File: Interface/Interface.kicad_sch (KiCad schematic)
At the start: 0 parts

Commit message: Finished the Design of Peripheral Circuit
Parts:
- added C1, C15, C16, C17, C24: 1u, symbol Device:C
- added C10, C13, C18, C21, C25, C3, C31, C32, C33, C9: 4.7u, symbol Device:C
- added C11, C12, C14, C19, C2, C20, C22, C23, C26, C4, C5, C6, C7, C8: 0.22u, symbol Device:C
- added C27, C28, C29, C30: 100n, symbol Device:C
- added L1: 4.7u, symbol Device:L
- added R1: 30k, symbol Device:R
- added U1: MIMXRT1011DAE5A, Package_QFP:LQFP-80_12x12mm_P0.5mm, symbol utils:MIMXRT1011DAE5A
- added U2: LM809, Package_TO_SOT_SMD:SOT-23, symbol Power_Supervisor:LM809
- added Y1: 24M, symbol Device:Crystal_GND24
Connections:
- new net: U1.22 (POR_B), U2.2 (~{RESET})
- new net: C16.1, U1.37 (XTALI), Y1.1
- new net: C17.1, U1.38 (XTALO), Y1.3
- new net: C23.1, R1.1, U1.15 (DCDC_PSWITCH)
- new net: L1.1, U1.19 (DCDC_LP)
- new net: C10.1, C11.1, U1.35 (VDD_HIGH_CAP)
- new net: C25.1, C26.1, U1.31 (VDD_USB_CAP)
- new net: U1.16 (VSS_1), U1.30 (VSS_2), U1.34 (NGND_KEL0), U1.54 (VSS_3), U1.78 (VSS_4)
- new net: C14.1, U1.26 (VDD_SNVS_CAP)
- new net: C12.1, C13.1, U1.40 (NVCC_PLL)
- new net +3.3V: C1.1, C15.1, C18.1, C19.1, C2.1, C20.1, C27.1, C28.1, C29.1, C3.1, C30.1, C31.1, C32.1, C33.1, C4.1, C5.1, R1.2, U1.17 (DCDC_IN_Q), U1.18 (DCDC_IN), U1.25 (VDD_SNVS_IN), U1.39 (VDD_HIGH_IN), U1.42 (VDDA_ADC_3P3/ADC_VREFH), U1.50 (NVCC_GPIO_2), U1.63 (NVCC_GPIO_3), U1.7 (NVCC_GPIO_1), U1.71 (NVCC_GPIO_4), U2.3 (VCC)
- new net GND: C1.2, C10.2, C11.2, C12.2, C13.2, C14.2, C15.2, C16.2, C17.2, C18.2, C19.2, C2.2, C20.2, C21.2, C22.2, C23.2, C24.2, C25.2, C26.2, C27.2, C28.2, C29.2, C3.2, C30.2, C31.2, C32.2, C33.2, C4.2, C5.2, C6.2, C7.2, C8.2, C9.2, U1.20 (DCDC_GND), U1.23 (TEST_MODE), U1.27 (RTC_XTALI), U1.41 (VSSA_ADC_3P3/ADC_VREFL), U2.1 (GND), Y1.2, Y1.4
- new net VBUS: C24.1, U1.29 (USB_OTG1_VBUS)
- new net VDD: C21.1, C22.1, C6.1, C7.1, C8.1, C9.1, L1.2, U1.14 (VDD_SOC_IN_3/DCDC_SENSE), U1.53 (VDD_SOC_IN_1), U1.77 (VDD_SOC_IN_2)
- no-connect marks 0 -> 4

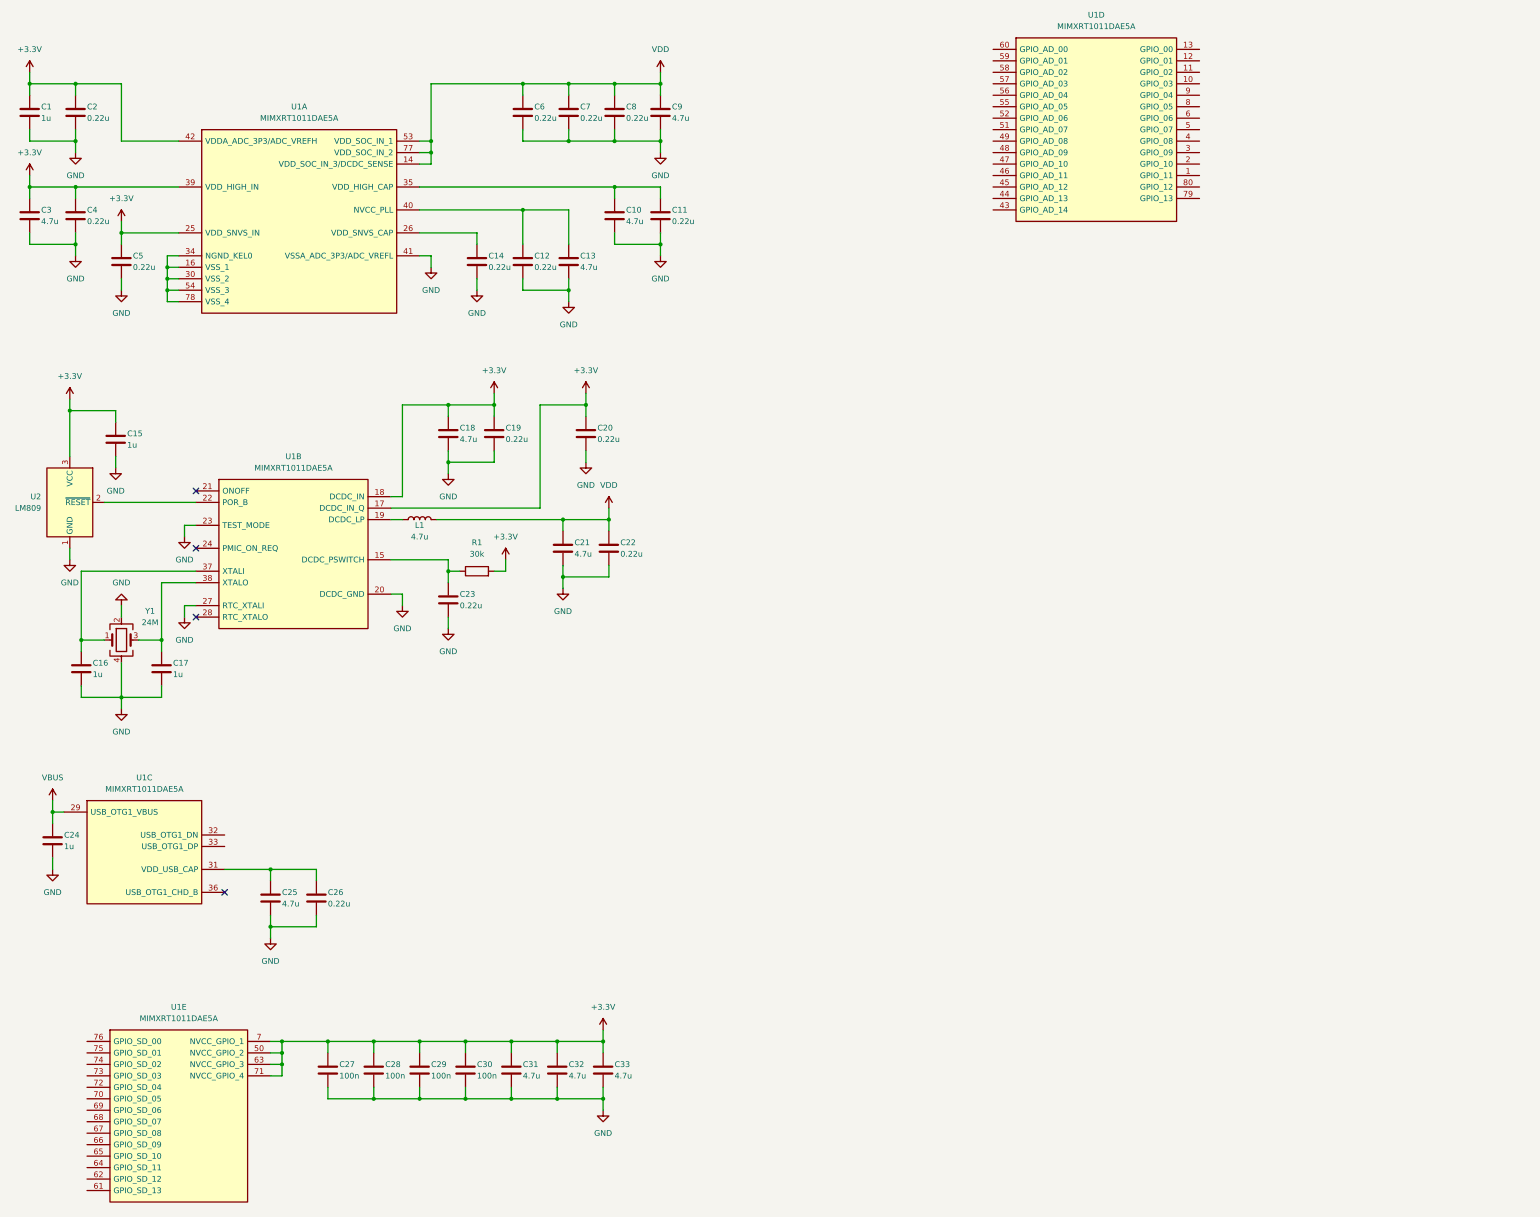
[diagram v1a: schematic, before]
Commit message: Finished Circuit Design of External Flash, Power Supply, etc.
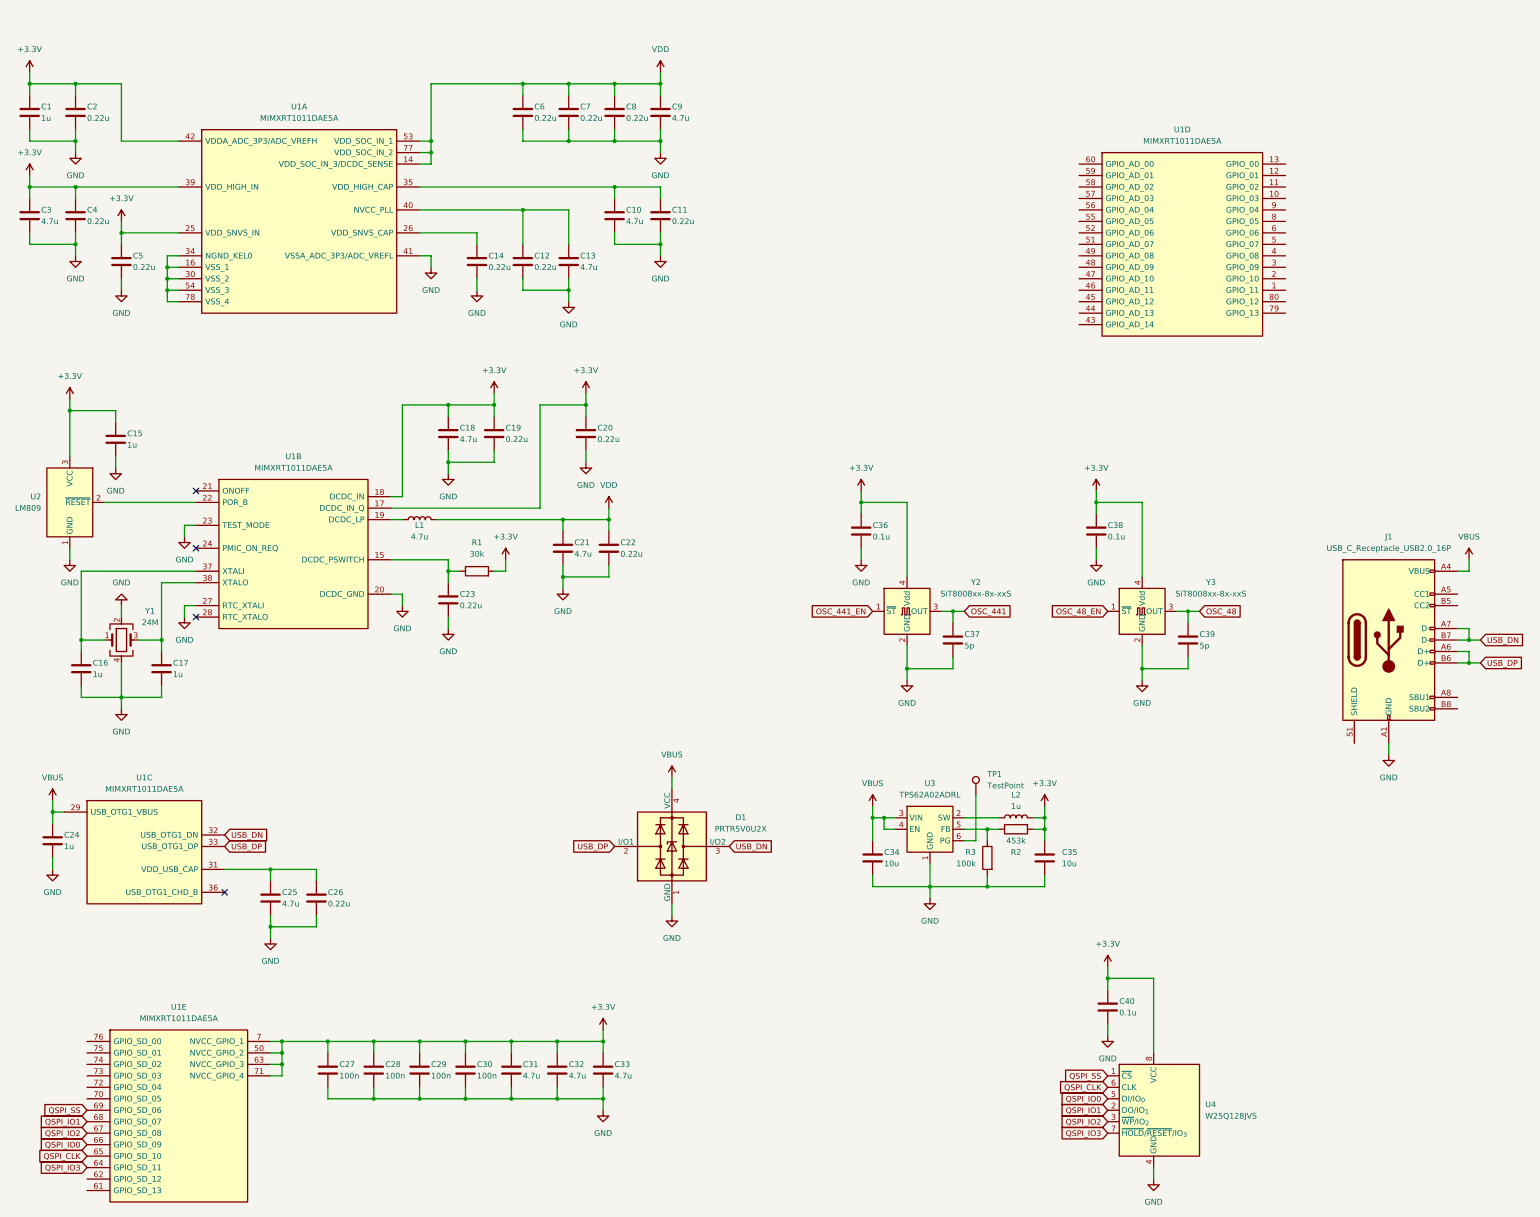
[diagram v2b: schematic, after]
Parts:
- added C34, C35: 10u, symbol Device:C
- added C36, C38, C40: 0.1u, symbol Device:C
- added C37, C39: 5p, symbol Device:C
- added D1: PRTR5V0U2X, Package_TO_SOT_SMD:SOT-143, symbol Power_Protection:PRTR5V0U2X
- added J1: USB_C_Receptacle_USB2.0_16P, symbol Connector:USB_C_Receptacle_USB2.0_16P
- added L2: 1u, symbol Device:L
- added R2: 453k, symbol Device:R
- added R3: 100k, symbol Device:R
- added TP1: TestPoint, TestPoint:TestPoint_Pad_D2.0mm, symbol Connector:TestPoint
- added U3: TPS62A02ADRL, Package_TO_SOT_SMD:SOT-563, symbol Regulator_Switching:TPS62A02ADRL
- added U4: W25Q128JVS, Package_SO:SOIC-8_5.3x5.3mm_P1.27mm, symbol Memory_Flash:W25Q128JVS
- added Y2, Y3: SiT8008xx-8x-xxS, Oscillator:Oscillator_SMD_SiT_PQFN-4Pin_7.0x5.0mm, symbol Oscillator:SiT8008xx-8x-xxS
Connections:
- net +3.3V: now also C35.1, C36.1, C38.1, C40.1, L2.2, R2.2, U4.8 (VCC), Y2.4 (Vdd), Y3.4 (Vdd)
- net GND: now also C34.2, C35.2, C36.2, C37.2, C38.2, C39.2, C40.2, D1.1 (GND), J1.A1 (GND), J1.A12 (GND), J1.B1 (GND), J1.B12 (GND), R3.2, U3.1 (GND), U4.4 (GND), Y2.2 (GND), Y3.2 (GND)
- net VBUS: now also C34.1, D1.4 (VCC), J1.A4 (VBUS), J1.A9 (VBUS), J1.B4 (VBUS), J1.B9 (VBUS), U3.3 (VIN), U3.4 (EN)
- net QSPI_IO3: now reaches U1.64 (GPIO_SD_11)
- net QSPI_IO3: now also U4.7 (~{HOLD}/~{RESET}/IO_{3})
- net QSPI_CLK: now reaches U1.65 (GPIO_SD_10)
- net QSPI_CLK: now also U4.6 (CLK)
- net QSPI_IO0: now reaches U1.66 (GPIO_SD_09)
- net QSPI_IO0: now also U4.5 (DI/IO_{0})
- net QSPI_IO2: now reaches U1.67 (GPIO_SD_08)
- net QSPI_IO2: now also U4.3 (~{WP}/IO_{2})
- net QSPI_IO1: now reaches U1.68 (GPIO_SD_07)
- net QSPI_IO1: now also U4.2 (DO/IO_{1})
- net QSPI_SS: now reaches U1.69 (GPIO_SD_06)
- net QSPI_SS: now also U4.1 (~{CS})
- net USB_DN: now reaches U1.32 (USB_OTG1_DN)
- net USB_DN: now also D1.3 (I/O2), J1.A7 (D-), J1.B7 (D-)
- net USB_DP: now reaches U1.33 (USB_OTG1_DP)
- net USB_DP: now also D1.2 (I/O1), J1.A6 (D+), J1.B6 (D+)
- new net: L2.1, U3.2 (SW)
- new net: R2.1, R3.1, U3.5 (FB)
- new net: TP1.1, U3.6 (PG)
- new net OSC_441: C37.1, Y2.3 (OUT)
- new net OSC_441_EN: Y2.1 (~{ST})
- new net OSC_48: C39.1, Y3.3 (OUT)
- new net OSC_48_EN: Y3.1 (~{ST})
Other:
- company: (none) -> Paranoid Workshop
- title: (none) -> PHASE-1/Digital_Audio_Interface
- moved on the sheet: U1D

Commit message: Peripheral Circuit Design Improvement
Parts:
- added C36: 0.22u, symbol Device:C
- added C42, C43: 1u, symbol Device:C
- added C44: 10u, symbol Device:C
- added R10, R7, R8, R9: 100k, symbol Device:R
- added R4: 10k, symbol Device:R
- added R5: 100, symbol Device:R
- added R6: 1.5k, symbol Device:R
- added SW1, SW2: SW_Push, symbol Switch:SW_Push
- added TP2: TestPoint, TestPoint:TestPoint_Pad_D2.0mm, symbol Connector:TestPoint
- added U5: XC6206PxxxMR, Package_TO_SOT_SMD:SOT-23-3, symbol Regulator_Linear:XC6206PxxxMR
- added U6: TS5A3159ADCK, Package_TO_SOT_SMD:SOT-363_SC-70-6, symbol Analog_Switch:TS5A3159ADCK
- added U7: FUSB302BMPX, Package_DFN_QFN:WQFN-14-1EP_2.5x2.5mm_P0.5mm_EP1.45x1.45mm, symbol Interface_USB:FUSB302BMPX
- C15: value 1u -> 0.1u
- renumbered C36 to C37, C37 to C38, C38 to C39, C39 to C40, C40 to C41
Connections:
- net +3.3V: now also C44.1, R6.1, R7.1, R8.2, SW2.2, U6.5 (V+); no longer C5.1, U1.25 (VDD_SNVS_IN)
- net GND: now also C36.2, C42.2, C43.2, C44.2, R10.2, R9.2, SW1.1, SW2.1, U5.1 (GND), U6.2 (GND)
- net VBUS: now also C42.1, U5.3 (VI); no longer U3.4 (EN)
- net at U1.22 (POR_B), U2.2 (~{RESET}): now also R8.1
- net PMIC_ON_REQ: now reaches U1.24 (PMIC_ON_REQ)
- net PMIC_ON_REQ: now also R4.1
- net BOOT_MODE0: now reaches U1.72 (GPIO_SD_04)
- net BOOT_MODE0: now also R9.1, U6.3
- net BOOT_MODE1: now reaches U1.73 (GPIO_SD_03)
- net BOOT_MODE1: now also R10.1, U6.1
- net at U1.36 (USB_OTG1_CHD_B): now also TP2.1
- new net: R7.2, U6.6
- new net: C36.1, R4.2, R5.2, U3.4 (EN)
- new net: R6.2, U6.4
- new net: R5.1, SW1.2
- new net: U7.1 (CC2), U7.14 (CC2)
- new net: U7.10 (CC1), U7.11 (CC1)
- new net: U7.15 (GND), U7.8 (GND), U7.9 (GND)
- new net: U7.3 (VDD), U7.4 (VDD)
- new net VDD_SNVS: C43.1, C5.1, U1.25 (VDD_SNVS_IN), U5.2 (VO)
- no-connect marks 4 -> 2
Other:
- moved on the sheet: C25, C26, C34, C35, C41, J1, L2, R2, R3, TP1, U1D, U3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

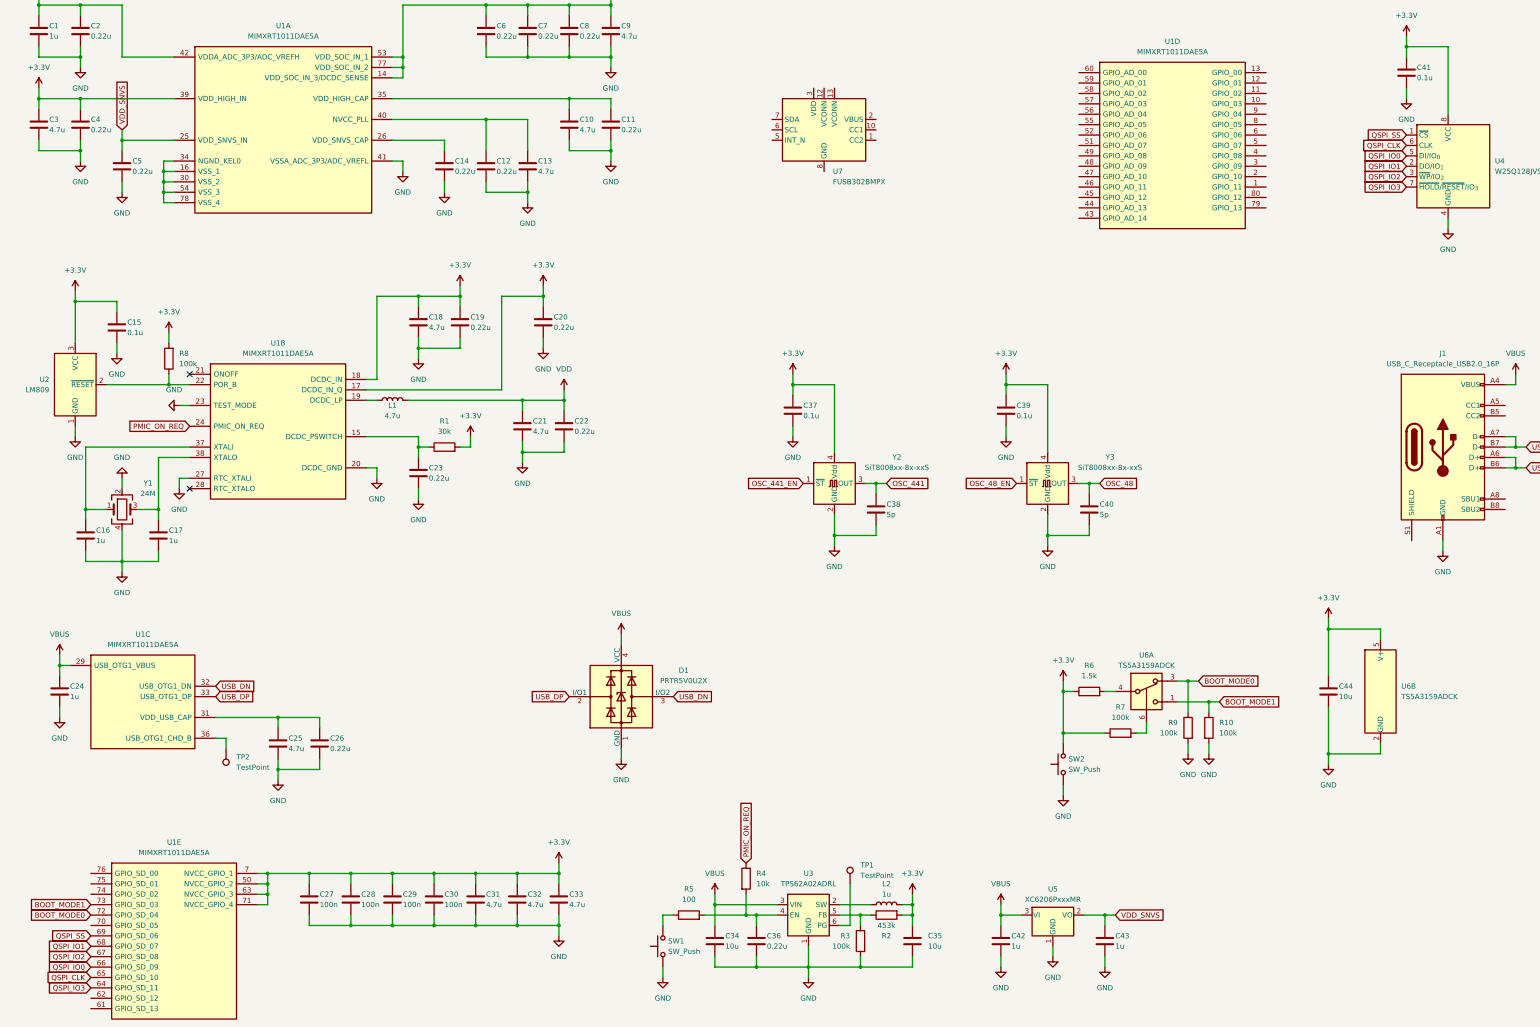
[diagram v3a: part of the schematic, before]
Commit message: Simplified Power Supply, Modified POR Circuit and Added DIP Switch for Boot Mode Select
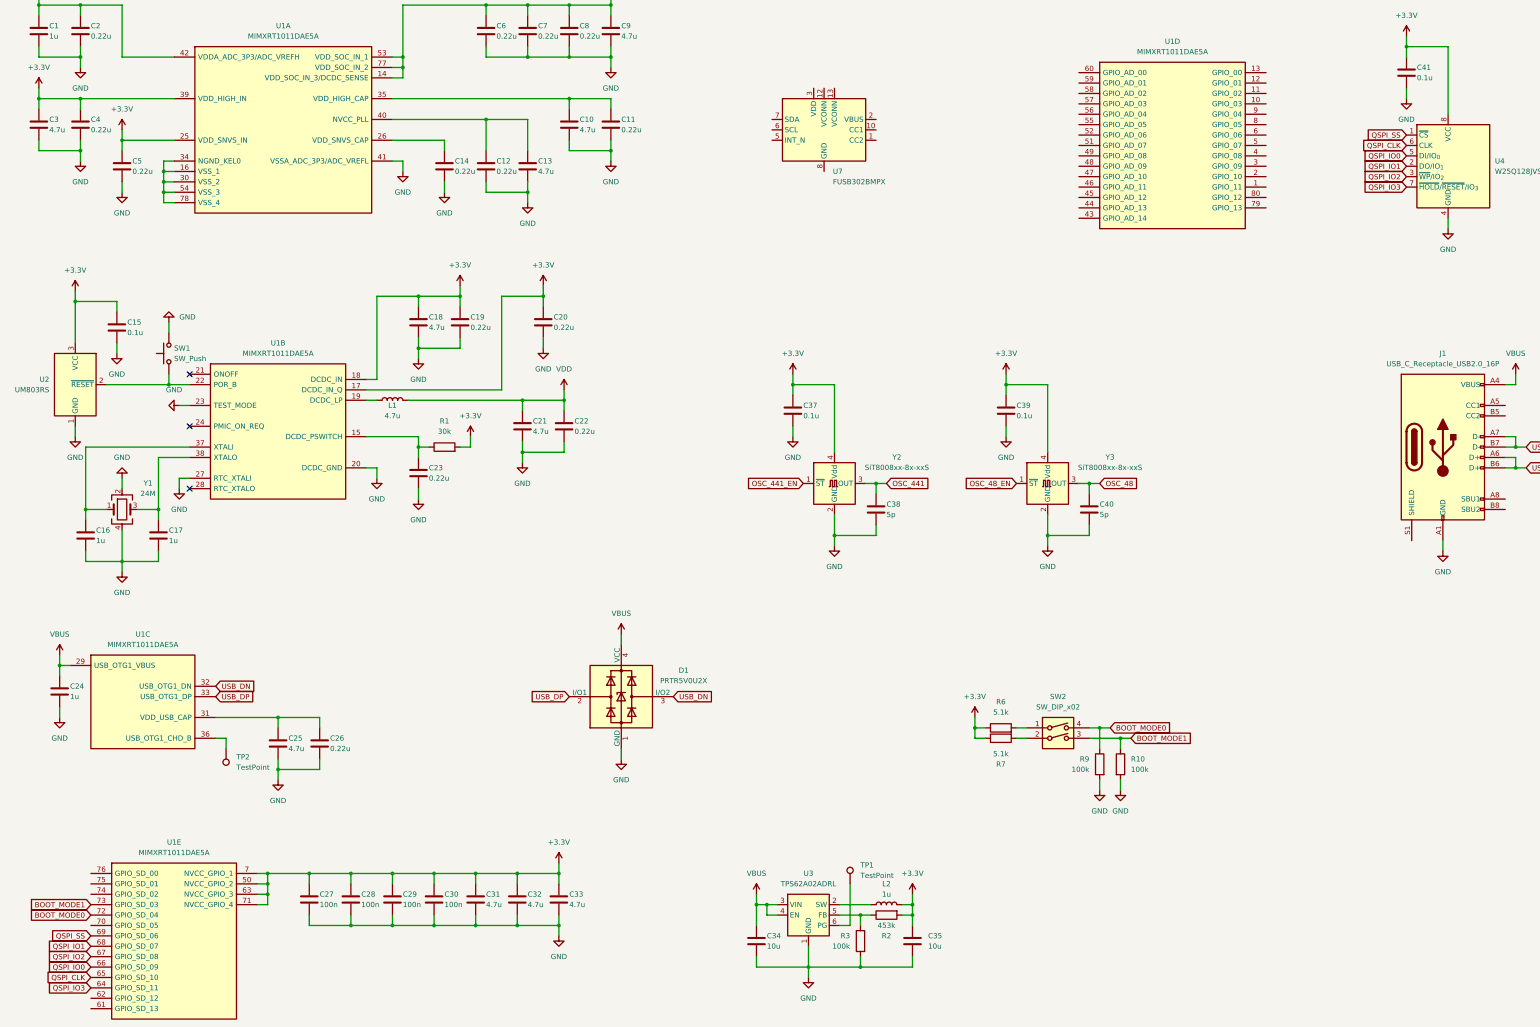
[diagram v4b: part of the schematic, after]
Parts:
- removed C36: 0.22u, symbol Device:C
- removed C42, C43: 1u, symbol Device:C
- removed C44: 10u, symbol Device:C
- removed R4: 10k, symbol Device:R
- removed R5: 100, symbol Device:R
- removed R8: 100k, symbol Device:R
- removed SW2: SW_Push, symbol Switch:SW_Push
- removed U2: LM809, Package_TO_SOT_SMD:SOT-23, symbol Power_Supervisor:LM809
- removed U5: XC6206PxxxMR, Package_TO_SOT_SMD:SOT-23-3, symbol Regulator_Linear:XC6206PxxxMR
- removed U6: TS5A3159ADCK, Package_TO_SOT_SMD:SOT-363_SC-70-6, symbol Analog_Switch:TS5A3159ADCK
- added SW2: SW_DIP_x02, symbol Switch:SW_DIP_x02
- added U2: UM803RS, Package_TO_SOT_SMD:SOT-23, symbol utils:UM803RS
- R6: value 1.5k -> 5.1k
- R7: value 100k -> 5.1k
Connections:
- net VDD_SNVS is gone; now on net +3.3V: C5.1, U1.25 (VDD_SNVS_IN)
- net +3.3V: now also U2.3 (VCC)
- net BOOT_MODE0: now also SW2.4
- net BOOT_MODE1: now also SW2.3
- net GND: now also SW1.2, U2.1 (GND); no longer SW1.1
- net VBUS: now also U3.4 (EN)
- net at U1.22 (POR_B): now also SW1.1, U2.2 (~{RESET})
- net at R7.2: now also SW2.2
- net at R6.2: now also SW2.1
- net PMIC_ON_REQ: no longer names the net of U1.24 (PMIC_ON_REQ)
- no-connect marks 2 -> 3
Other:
- moved on the sheet: C34, R10, R6, R7, R9, SW1

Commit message: Detail Improvement
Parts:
- removed Y2, Y3: SiT8008xx-8x-xxS, Oscillator:Oscillator_SMD_SiT_PQFN-4Pin_7.0x5.0mm, symbol Oscillator:SiT8008xx-8x-xxS
- added TP3: TestPoint, TestPoint:TestPoint_Pad_D2.0mm, symbol Connector:TestPoint
- added Y2, Y3: KC2520Z, Oscillator:Oscillator_SMD_Kyocera_KC2520Z-4Pin_2.5x2.0mm, symbol Oscillator:KC2520Z
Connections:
- net +3.3V: now also Y2.4 (VCC), Y3.4 (VCC)
- net GND: now also Y2.2 (GND), Y3.2 (GND)
- net OSC_441: now also Y2.3 (CLK)
- net OSC_441_EN: now also Y2.1 (INH)
- net OSC_48: now also Y3.3 (CLK)
- net OSC_48_EN: now also Y3.1 (INH)
- net at U1.62 (GPIO_SD_12): now also TP3.1
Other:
- moved on the sheet: C38, C40
